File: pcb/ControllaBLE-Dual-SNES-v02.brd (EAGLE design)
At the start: 100 x 61 mm, 3 parts

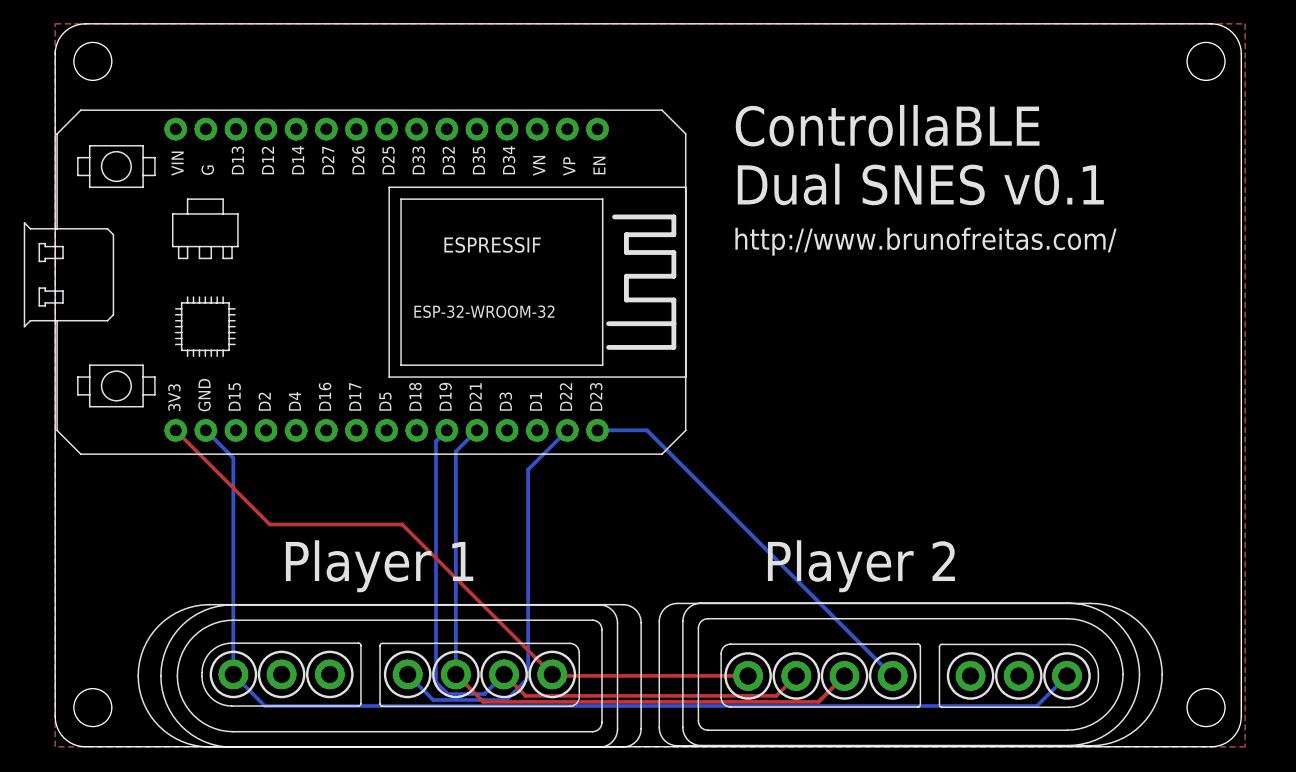
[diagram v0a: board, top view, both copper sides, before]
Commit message: Fixing wrong SNES connector position in the PCB
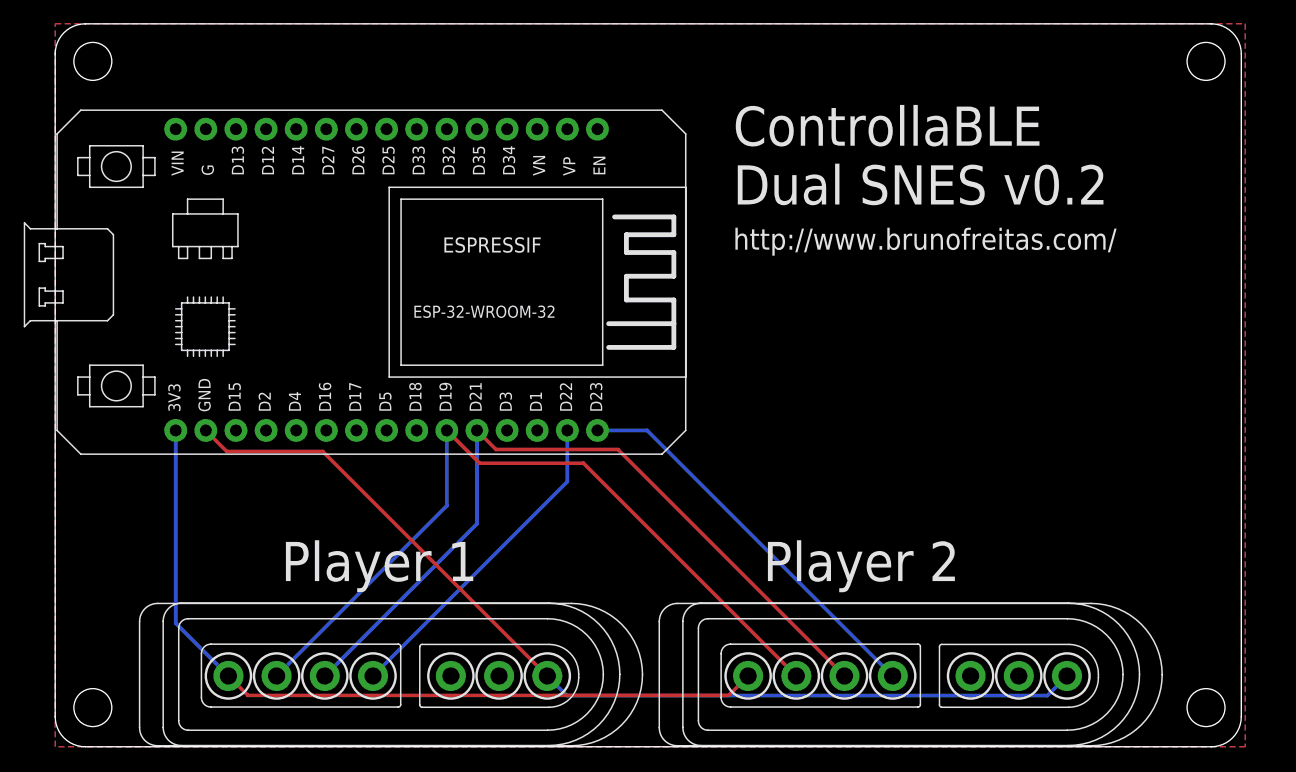
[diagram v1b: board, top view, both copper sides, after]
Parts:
- moved U$1 28.5 mm to (14.6, 1.91), turned to 0 degrees
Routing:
- net GND: track 94.0 -> 82.5 mm
- net 3V3: track 56.8 -> 67.7 mm
- net CLOCK: track 54.5 -> 64.7 mm
- net LATCH: track 55.9 -> 65.6 mm
- net P1_DATA: track 34.1 -> 27.5 mm
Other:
- board text added: "ControllaBLE Dual SNES v0.2"
- board text removed: "ControllaBLE Dual SNES v0.1"
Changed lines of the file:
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@@
 <hole x="97.028" y="3.302" drill="3.2"/>
 <text x="57.15" y="45.72" size="3.302" layer="21" font="vector" ratio="13">ControllaBLE
-Dual SNES v0.1</text>
+Dual SNES v0.2</text>
 <text x="57.15" y="41.91" size="1.778" layer="21" font="vector">http://www.brunofreitas.com/</text>
 <text x="19.05" y="13.97" size="3.302" layer="21" font="vector" ratio="13">Player 1</text>
@@
 </autorouter>
 <elements>
-<element name="U$1" library="gamepad-conn" package="SNESCONN" value="SNESCONN" x="41.91" y="10.16" rot="R180"/>
+<element name="U$1" library="gamepad-conn" package="SNESCONN" value="SNESCONN" x="14.605" y="1.905"/>
 <element name="BOARD1" library="ESP32-DEVKITV1" package="ESP32-DEVKITV1" value="ESP32DEVKITV1" x="10.16" y="26.67" smashed="yes">
 <attribute name="ESP32-DEVKITV1" value="" x="10.16" y="26.67" size="1.778" layer="27" display="off"/>
@@
 <contactref element="U$2" pad="GND"/>
 <contactref element="BOARD1" pad="GND@1"/>
-<wire x1="15.026" y1="6.096" x2="17.6896" y2="3.4324" width="0.3048" layer="16"/>
-<wire x1="17.6896" y1="3.4324" x2="82.7674" y2="3.4324" width="0.3048" layer="16"/>
-<wire x1="82.7674" y1="3.4324" x2="85.304" y2="5.969" width="0.3048" layer="16"/>
-<wire x1="15.026" y1="6.096" x2="15.026" y2="24.344" width="0.3048" layer="16"/>
-<wire x1="15.026" y1="24.344" x2="12.7" y2="26.67" width="0.3048" layer="16"/>
+<wire x1="85.304" y1="5.969" x2="83.6495" y2="4.3145" width="0.3048" layer="16"/>
+<wire x1="83.6495" y1="4.3145" x2="43.1435" y2="4.3145" width="0.3048" layer="16"/>
+<wire x1="43.1435" y1="4.3145" x2="41.489" y2="5.969" width="0.3048" layer="16"/>
+<wire x1="41.489" y1="5.969" x2="22.5624" y2="24.8956" width="0.3048" layer="1"/>
+<wire x1="22.5624" y1="24.8956" x2="14.4744" y2="24.8956" width="0.3048" layer="1"/>
+<wire x1="14.4744" y1="24.8956" x2="12.7" y2="26.67" width="0.3048" layer="1"/>
 <polygon width="0.4064" layer="16" spacing="0.6096" pour="hatch" isolate="0.4064">
 <vertex x="0" y="60.96"/>
@@
 <contactref element="U$2" pad="CLOCK"/>
 <contactref element="BOARD1" pad="D19"/>
-<wire x1="37.846" y1="6.096" x2="36.1987" y2="4.4487" width="0.3048" layer="16"/>
-<wire x1="36.1987" y1="4.4487" x2="33.099" y2="4.4487" width="0.3048" layer="16"/>
-<wire x1="33.099" y1="4.4487" x2="32.1057" y2="5.442" width="0.3048" layer="16"/>
-<wire x1="32.1057" y1="5.442" x2="32.1057" y2="25.7557" width="0.3048" layer="16"/>
-<wire x1="32.1057" y1="25.7557" x2="33.02" y2="26.67" width="0.3048" layer="16"/>
-<wire x1="62.484" y1="5.969" x2="60.808" y2="4.293" width="0.3048" layer="1"/>
-<wire x1="60.808" y1="4.293" x2="39.649" y2="4.293" width="0.3048" layer="1"/>
-<wire x1="39.649" y1="4.293" x2="37.846" y2="6.096" width="0.3048" layer="1"/>
+<wire x1="62.484" y1="5.969" x2="44.545" y2="23.908" width="0.3048" layer="1"/>
+<wire x1="44.545" y1="23.908" x2="35.782" y2="23.908" width="0.3048" layer="1"/>
+<wire x1="35.782" y1="23.908" x2="33.02" y2="26.67" width="0.3048" layer="1"/>
+<wire x1="18.669" y1="5.969" x2="33.02" y2="20.32" width="0.3048" layer="16"/>
+<wire x1="33.02" y1="20.32" x2="33.02" y2="26.67" width="0.3048" layer="16"/>
 </signal>
 <signal name="LATCH">
@@
 <contactref element="U$2" pad="LATCH"/>
 <contactref element="BOARD1" pad="D21"/>
-<wire x1="33.782" y1="6.096" x2="33.782" y2="24.892" width="0.3048" layer="16"/>
-<wire x1="33.782" y1="24.892" x2="35.56" y2="26.67" width="0.3048" layer="16"/>
-<wire x1="33.782" y1="6.096" x2="36.0932" y2="3.7848" width="0.3048" layer="1"/>
-<wire x1="36.0932" y1="3.7848" x2="64.3638" y2="3.7848" width="0.3048" layer="1"/>
-<wire x1="64.3638" y1="3.7848" x2="66.548" y2="5.969" width="0.3048" layer="1"/>
+<wire x1="66.548" y1="5.969" x2="47.4577" y2="25.0593" width="0.3048" layer="1"/>
+<wire x1="47.4577" y1="25.0593" x2="37.1707" y2="25.0593" width="0.3048" layer="1"/>
+<wire x1="37.1707" y1="25.0593" x2="35.56" y2="26.67" width="0.3048" layer="1"/>
+<wire x1="22.733" y1="5.969" x2="35.56" y2="18.796" width="0.3048" layer="16"/>
+<wire x1="35.56" y1="18.796" x2="35.56" y2="26.67" width="0.3048" layer="16"/>
 </signal>
 <signal name="P1_DATA">
 <contactref element="U$1" pad="DATA"/>
 <contactref element="BOARD1" pad="D22"/>
-<wire x1="29.718" y1="6.096" x2="31.8735" y2="3.9405" width="0.3048" layer="16"/>
-<wire x1="31.8735" y1="3.9405" x2="38.0273" y2="3.9405" width="0.3048" layer="16"/>
-<wire x1="38.0273" y1="3.9405" x2="39.8781" y2="5.7913" width="0.3048" layer="16"/>
-<wire x1="39.8781" y1="5.7913" x2="39.8781" y2="23.3681" width="0.3048" layer="16"/>
-<wire x1="39.8781" y1="23.3681" x2="43.18" y2="26.67" width="0.3048" layer="16"/>
+<wire x1="26.797" y1="5.969" x2="43.18" y2="22.352" width="0.3048" layer="16"/>
+<wire x1="43.18" y1="22.352" x2="43.18" y2="26.67" width="0.3048" layer="16"/>
 </signal>
 <signal name="3V3">
@@
 <contactref element="U$2" pad="5V"/>
 <contactref element="BOARD1" pad="3V3"/>
-<wire x1="41.91" y1="6.096" x2="29.2638" y2="18.7422" width="0.3048" layer="1"/>
-<wire x1="29.2638" y1="18.7422" x2="18.0878" y2="18.7422" width="0.3048" layer="1"/>
-<wire x1="18.0878" y1="18.7422" x2="10.16" y2="26.67" width="0.3048" layer="1"/>
-<wire x1="58.42" y1="5.969" x2="42.037" y2="5.969" width="0.3048" layer="1"/>
-<wire x1="42.037" y1="5.969" x2="41.91" y2="6.096" width="0.3048" layer="1"/>
+<wire x1="14.605" y1="5.969" x2="16.2413" y2="4.3327" width="0.3048" layer="1"/>
+<wire x1="16.2413" y1="4.3327" x2="56.7837" y2="4.3327" width="0.3048" layer="1"/>
+<wire x1="56.7837" y1="4.3327" x2="58.42" y2="5.969" width="0.3048" layer="1"/>
+<wire x1="14.605" y1="5.969" x2="10.16" y2="10.414" width="0.3048" layer="16"/>
+<wire x1="10.16" y1="10.414" x2="10.16" y2="26.67" width="0.3048" layer="16"/>
 </signal>
 <signal name="P2_DATA">
